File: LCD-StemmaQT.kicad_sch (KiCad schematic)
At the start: 18 parts, among them J101 STEMMA QT, J102 LCD, J103 BL enable, Q101 MMBT3904, U101 PCF8574TS

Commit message: Non functional corrections on PCB
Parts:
- JP101: value SolderJumper_2_Open -> A0
- JP102: value SolderJumper_2_Open -> A1
- JP103: value SolderJumper_2_Open -> A2
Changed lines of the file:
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@@
   )
   (symbol (lib_id "Device:R") (at 73.66 41.91 0) (unit 1)
-    (in_bom yes) (on_board yes) (fields_autoplaced)
+    (in_bom yes) (on_board yes)
     (property "Reference" "R105" (id 0) (at 75.565 40.6399 0)
       (effects (font (size 1.27 1.27)) (justify left))
@@
       (effects (font (size 1.27 1.27)) hide)
     )
-    (property "LCSC" "C25804" (id 4) (at 73.66 41.91 0))
+    (property "LCSC" "C25804" (id 4) (at 79.375 45.085 0))
     (pin "1")
     (pin "2")
@@
     )
     (property "Footprint" "Connector_PinHeader_2.54mm:PinHeader_1x16_P2.54mm_Vertical" (id 2) (at 252.73 97.1549 0)
-      (effects (font (size 1.27 1.27)) (justify left))
+      (effects (font (size 1.27 1.27)) (justify left) hide)
     )
     (property "Datasheet" "~" (id 3) (at 249.555 93.345 0)
@@
   )
   (symbol (lib_id "Interface_Expansion:PCF8574TS") (at 125.73 115.57 0) (unit 1)
-    (in_bom yes) (on_board yes) (fields_autoplaced)
-    (property "Reference" "U101" (id 0) (at 127.7494 95.25 0)
-      (effects (font (size 1.27 1.27)) (justify left))
-    )
-    (property "Value" "PCF8574TS" (id 1) (at 127.7494 97.79 0)
+    (in_bom yes) (on_board yes)
+    (property "Reference" "U101" (id 0) (at 127.7494 94.615 0)
+      (effects (font (size 1.27 1.27)) (justify left))
+    )
+    (property "Value" "PCF8574TS" (id 1) (at 127.7494 97.155 0)
       (effects (font (size 1.27 1.27)) (justify left))
     )
@@
       (effects (font (size 1.27 1.27)) hide)
     )
-    (property "LCSC" "C57790" (id 4) (at 125.73 115.57 0))
+    (property "LCSC" "C57790" (id 4) (at 131.445 99.06 0))
     (pin "1")
     (pin "10")
@@
   )
   (symbol (lib_id "Device:R") (at 64.135 41.91 0) (unit 1)
-    (in_bom yes) (on_board yes) (fields_autoplaced)
+    (in_bom yes) (on_board yes)
     (property "Reference" "R104" (id 0) (at 66.04 40.6399 0)
       (effects (font (size 1.27 1.27)) (justify left))
@@
       (effects (font (size 1.27 1.27)) hide)
     )
-    (property "LCSC" "C25804" (id 4) (at 64.135 41.91 0))
+    (property "LCSC" "C25804" (id 4) (at 69.85 45.085 0))
     (pin "1")
     (pin "2")
@@
   )
   (symbol (lib_id "Device:R") (at 100.33 41.91 0) (unit 1)
-    (in_bom yes) (on_board yes) (fields_autoplaced)
+    (in_bom yes) (on_board yes)
     (property "Reference" "R106" (id 0) (at 102.235 40.6399 0)
       (effects (font (size 1.27 1.27)) (justify left))
@@
       (effects (font (size 1.27 1.27)) hide)
     )
-    (property "LCSC" "C23162" (id 4) (at 100.33 41.91 0))
+    (property "LCSC" "C23162" (id 4) (at 106.045 45.085 0))
     (pin "1")
     (pin "2")
   )
   (symbol (lib_id "Device:R") (at 36.195 41.91 0) (unit 1)
-    (in_bom yes) (on_board yes) (fields_autoplaced)
+    (in_bom yes) (on_board yes)
     (property "Reference" "R102" (id 0) (at 38.1 40.6399 0)
       (effects (font (size 1.27 1.27)) (justify left))
@@
       (effects (font (size 1.27 1.27)) hide)
     )
-    (property "LCSC" "C21190" (id 4) (at 36.195 41.91 0))
+    (property "LCSC" "C21190" (id 4) (at 41.91 45.085 0))
     (pin "1")
     (pin "2")
@@
   )
   (symbol (lib_id "Transistor_BJT:MMBT3904") (at 187.325 59.69 0) (unit 1)
-    (in_bom yes) (on_board yes) (fields_autoplaced)
+    (in_bom yes) (on_board yes)
     (property "Reference" "Q101" (id 0) (at 193.04 58.4199 0)
       (effects (font (size 1.27 1.27)) (justify left))
@@
       (effects (font (size 1.27 1.27)) (justify left) hide)
     )
-    (property "LCSC" "C411758" (id 4) (at 187.325 59.69 0))
+    (property "LCSC" "C411758" (id 4) (at 197.485 63.5 0))
     (pin "1")
     (pin "2")
@@
   )
   (symbol (lib_id "Jumper:SolderJumper_2_Open") (at 64.135 59.69 90) (unit 1)
-    (in_bom yes) (on_board yes) (fields_autoplaced)
-    (property "Reference" "JP102" (id 0) (at 58.42 59.69 0))
-    (property "Value" "SolderJumper_2_Open" (id 1) (at 60.96 59.69 0)
-      (effects (font (size 1.27 1.27)) hide)
-    )
+    (in_bom yes) (on_board yes)
+    (property "Reference" "JP102" (id 0) (at 60.325 59.69 0))
+    (property "Value" "A1" (id 1) (at 62.23 59.69 0))
     (property "Footprint" "Jumper:SolderJumper-2_P1.3mm_Open_TrianglePad1.0x1.5mm" (id 2) (at 64.135 59.69 0)
       (effects (font (size 1.27 1.27)) hide)
@@
   )
   (symbol (lib_id "Device:R") (at 112.395 41.91 0) (unit 1)
-    (in_bom yes) (on_board yes) (fields_autoplaced)
+    (in_bom yes) (on_board yes)
     (property "Reference" "R107" (id 0) (at 114.3 40.6399 0)
       (effects (font (size 1.27 1.27)) (justify left))
@@
       (effects (font (size 1.27 1.27)) hide)
     )
-    (property "LCSC" "C23162" (id 4) (at 112.395 41.91 0))
+    (property "LCSC" "C23162" (id 4) (at 118.11 45.085 0))
     (pin "1")
     (pin "2")
   )
   (symbol (lib_id "Device:R") (at 53.975 41.91 0) (unit 1)
-    (in_bom yes) (on_board yes) (fields_autoplaced)
+    (in_bom yes) (on_board yes)
     (property "Reference" "R103" (id 0) (at 55.88 40.6399 0)
       (effects (font (size 1.27 1.27)) (justify left))
@@
       (effects (font (size 1.27 1.27)) hide)
     )
-    (property "LCSC" "C25804" (id 4) (at 53.975 41.91 0))
+    (property "LCSC" "C25804" (id 4) (at 59.69 45.085 0))
     (pin "1")
     (pin "2")
@@
   )
   (symbol (lib_id "Jumper:SolderJumper_2_Open") (at 73.66 59.69 90) (unit 1)
-    (in_bom yes) (on_board yes) (fields_autoplaced)
-    (property "Reference" "JP103" (id 0) (at 67.945 59.69 0))
-    (property "Value" "SolderJumper_2_Open" (id 1) (at 70.485 59.69 0)
-      (effects (font (size 1.27 1.27)) hide)
-    )
+    (in_bom yes) (on_board yes)
+    (property "Reference" "JP103" (id 0) (at 69.85 59.69 0))
+    (property "Value" "A2" (id 1) (at 71.755 59.69 0))
     (property "Footprint" "Jumper:SolderJumper-2_P1.3mm_Open_TrianglePad1.0x1.5mm" (id 2) (at 73.66 59.69 0)
       (effects (font (size 1.27 1.27)) hide)
@@
       (effects (font (size 1.27 1.27)) hide)
     )
-    (property "LCSC" "C23162" (id 4) (at 176.53 41.91 0))
+    (property "LCSC" "C23162" (id 4) (at 182.88 42.545 0))
     (pin "1")
     (pin "2")
@@
   (symbol (lib_id "Device:LED") (at 36.195 59.69 90) (unit 1)
     (in_bom yes) (on_board yes)
-    (property "Reference" "D101" (id 0) (at 29.21 61.2775 0))
-    (property "Value" "LED" (id 1) (at 31.75 61.2775 0))
+    (property "Reference" "D101" (id 0) (at 31.115 57.785 90))
+    (property "Value" "LED" (id 1) (at 30.48 60.325 90))
     (property "Footprint" "LED_SMD:LED_0603_1608Metric_Pad1.05x0.95mm_HandSolder" (id 2) (at 36.195 59.69 0)
       (effects (font (size 1.27 1.27)) hide)
@@
       (effects (font (size 1.27 1.27)) hide)
     )
-    (property "LCSC" "C2286" (id 4) (at 36.195 59.69 0))
+    (property "LCSC" "C2286" (id 4) (at 31.75 62.23 90))
     (pin "1")
     (pin "2")
@@
       (effects (font (size 1.27 1.27)) hide)
     )
-    (property "LCSC" "C14663" (id 4) (at 130.175 41.91 0))
+    (property "LCSC" "C14663" (id 4) (at 137.795 45.085 0))
     (pin "1")
     (pin "2")
   )
   (symbol (lib_id "Jumper:SolderJumper_2_Open") (at 53.975 59.69 90) (unit 1)
-    (in_bom yes) (on_board yes) (fields_autoplaced)
-    (property "Reference" "JP101" (id 0) (at 48.26 59.69 0))
-    (property "Value" "SolderJumper_2_Open" (id 1) (at 50.8 59.69 0)
-      (effects (font (size 1.27 1.27)) hide)
-    )
+    (in_bom yes) (on_board yes)
+    (property "Reference" "JP101" (id 0) (at 50.165 59.69 0))
+    (property "Value" "A0" (id 1) (at 52.07 59.69 0))
     (property "Footprint" "Jumper:SolderJumper-2_P1.3mm_Open_TrianglePad1.0x1.5mm" (id 2) (at 53.975 59.69 0)
       (effects (font (size 1.27 1.27)) hide)
@@
     )
     (path "/fcee0fb2-df32-4024-ba70-44a5ab719340"
-      (reference "JP101") (unit 1) (value "SolderJumper_2_Open") (footprint "Jumper:SolderJumper-2_P1.3mm_Open_TrianglePad1.0x1.5mm")
+      (reference "JP101") (unit 1) (value "A0") (footprint "Jumper:SolderJumper-2_P1.3mm_Open_TrianglePad1.0x1.5mm")
     )
     (path "/82161366-81a3-4ef5-a36a-e224ed535ca4"
-      (reference "JP102") (unit 1) (value "SolderJumper_2_Open") (footprint "Jumper:SolderJumper-2_P1.3mm_Open_TrianglePad1.0x1.5mm")
+      (reference "JP102") (unit 1) (value "A1") (footprint "Jumper:SolderJumper-2_P1.3mm_Open_TrianglePad1.0x1.5mm")
     )
     (path "/d61cd04e-b64c-459d-9e89-c068997ca3cf"
-      (reference "JP103") (unit 1) (value "SolderJumper_2_Open") (footprint "Jumper:SolderJumper-2_P1.3mm_Open_TrianglePad1.0x1.5mm")
+      (reference "JP103") (unit 1) (value "A2") (footprint "Jumper:SolderJumper-2_P1.3mm_Open_TrianglePad1.0x1.5mm")
     )
     (path "/5b3858e1-b0b8-469d-8aa5-091532f0b5b8"

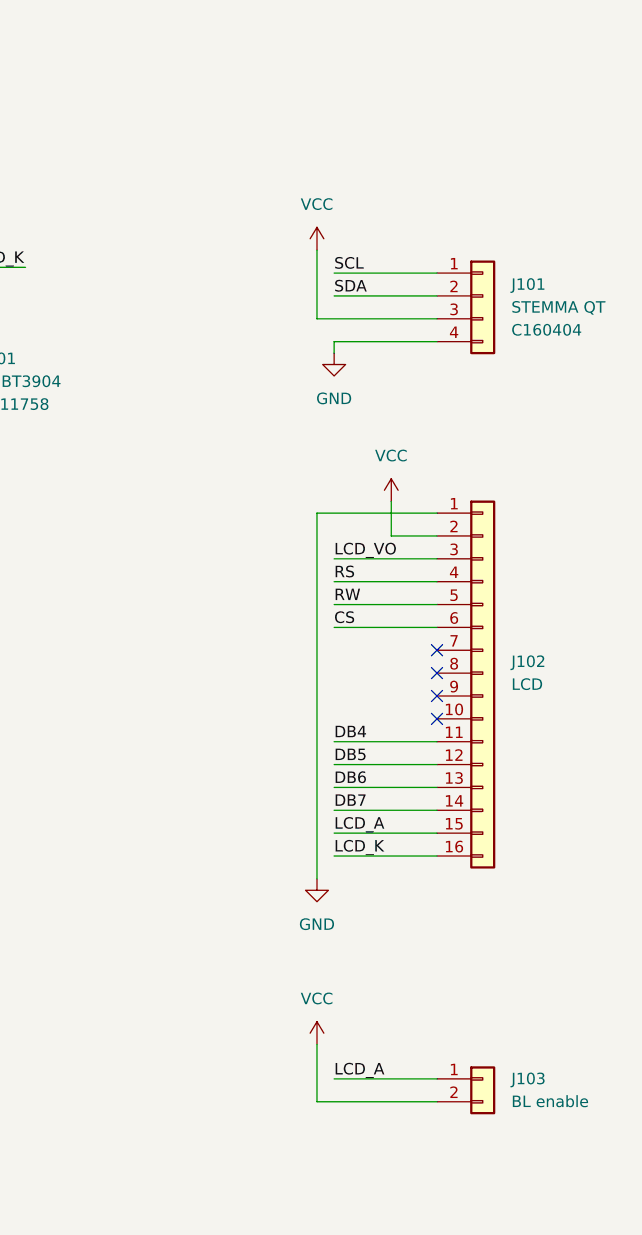
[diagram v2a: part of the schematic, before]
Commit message: Stemma QT footprint corrected
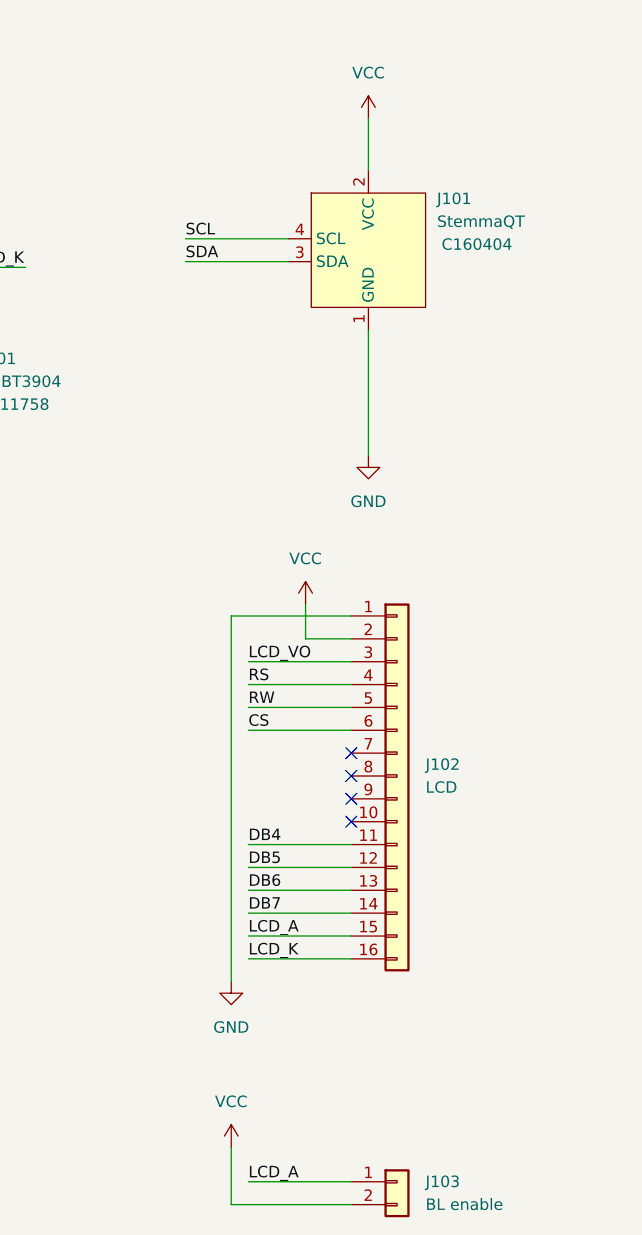
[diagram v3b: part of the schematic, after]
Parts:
- removed J101: STEMMA QT, Connector_JST:JST_SH_BM04B-SRSS-TB_1x04-1MP_P1.00mm_Vertical, symbol Connector_Generic:Conn_01x04
- added J101: StemmaQT, Connector_JST:JST_SH_SM04B-SRSS-TB_1x04-1MP_P1.00mm_Horizontal, symbol Resterampe:StemmaQT
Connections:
- net GND: now also J101.1 (GND)
- net SCL: now also J101.4 (SCL)
- net SDA: now also J101.3 (SDA)
- net VCC: now also J101.2 (VCC)
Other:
- moved on the sheet: J102, J103

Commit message: Documentation updated
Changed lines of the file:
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@@
   (junction (at 53.975 34.925) (diameter 0) (color 0 0 0 0)
+  )
+  (junction (at 215.9 86.995) (diameter 0) (color 0 0 0 0)
+  )
+  (junction (at 231.775 89.535) (diameter 0) (color 0 0 0 0)
   )
   (junction (at 53.975 48.26) (diameter 0) (color 0 0 0 0)
@@
     (stroke (width 0) (type default) (color 0 0 0 0))
   )
+  (wire (pts (xy 231.775 89.535) (xy 221.615 89.535))
+    (stroke (width 0) (type default) (color 0 0 0 0))
+  )
+  (wire (pts (xy 215.9 86.995) (xy 215.9 127.635))
+    (stroke (width 0) (type default) (color 0 0 0 0))
+  )
   (wire (pts (xy 53.975 34.925) (xy 53.975 38.1))
     (stroke (width 0) (type default) (color 0 0 0 0))
   )
-  (wire (pts (xy 234.95 86.995) (xy 221.615 86.995))
-    (stroke (width 0) (type default) (color 0 0 0 0))
-  )
-  (wire (pts (xy 229.87 89.535) (xy 229.87 85.725))
+  (wire (pts (xy 234.95 86.995) (xy 215.9 86.995))
+    (stroke (width 0) (type default) (color 0 0 0 0))
+  )
+  (wire (pts (xy 221.615 89.535) (xy 221.615 85.725))
     (stroke (width 0) (type default) (color 0 0 0 0))
   )
@@
     (stroke (width 0) (type default) (color 0 0 0 0))
   )
-  (wire (pts (xy 221.615 86.995) (xy 221.615 127.635))
-    (stroke (width 0) (type default) (color 0 0 0 0))
-  )
   (wire (pts (xy 100.33 45.72) (xy 100.33 48.26))
     (stroke (width 0) (type default) (color 0 0 0 0))
@@
     (stroke (width 0) (type default) (color 0 0 0 0))
   )
-  (wire (pts (xy 234.95 89.535) (xy 229.87 89.535))
+  (wire (pts (xy 234.95 89.535) (xy 231.775 89.535))
     (stroke (width 0) (type default) (color 0 0 0 0))
   )
@@
     (stroke (width 0) (type default) (color 0 0 0 0))
   )
+  (wire (pts (xy 210.82 86.995) (xy 210.82 85.725))
+    (stroke (width 0) (type default) (color 0 0 0 0))
+  )
   (wire (pts (xy 36.195 31.75) (xy 36.195 38.1))
     (stroke (width 0) (type default) (color 0 0 0 0))
@@
     (stroke (width 0) (type default) (color 0 0 0 0))
   )
+  (wire (pts (xy 215.9 86.995) (xy 210.82 86.995))
+    (stroke (width 0) (type default) (color 0 0 0 0))
+  )
   (wire (pts (xy 64.135 45.72) (xy 64.135 50.8))
     (stroke (width 0) (type default) (color 0 0 0 0))
@@
   )
   (wire (pts (xy 73.66 45.72) (xy 73.66 53.34))
+    (stroke (width 0) (type default) (color 0 0 0 0))
+  )
+  (wire (pts (xy 231.775 85.725) (xy 231.775 89.535))
     (stroke (width 0) (type default) (color 0 0 0 0))
   )
@@
     (pin "1")
   )
+  (symbol (lib_id "power:PWR_FLAG") (at 210.82 85.725 0) (unit 1)
+    (in_bom yes) (on_board yes) (fields_autoplaced)
+    (property "Reference" "#FLG0101" (id 0) (at 210.82 83.82 0)
+      (effects (font (size 1.27 1.27)) hide)
+    )
+    (property "Value" "PWR_FLAG" (id 1) (at 210.82 80.01 0))
+    (property "Footprint" "" (id 2) (at 210.82 85.725 0)
+      (effects (font (size 1.27 1.27)) hide)
+    )
+    (property "Datasheet" "~" (id 3) (at 210.82 85.725 0)
+      (effects (font (size 1.27 1.27)) hide)
+    )
+    (pin "1")
+  )
   (symbol (lib_id "power:VCC") (at 53.975 31.75 0) (unit 1)
     (in_bom yes) (on_board yes)
@@
     (pin "2")
   )
+  (symbol (lib_id "power:PWR_FLAG") (at 231.775 85.725 0) (unit 1)
+    (in_bom yes) (on_board yes) (fields_autoplaced)
+    (property "Reference" "#FLG0102" (id 0) (at 231.775 83.82 0)
+      (effects (font (size 1.27 1.27)) hide)
+    )
+    (property "Value" "PWR_FLAG" (id 1) (at 231.775 80.01 0))
+    (property "Footprint" "" (id 2) (at 231.775 85.725 0)
+      (effects (font (size 1.27 1.27)) hide)
+    )
+    (property "Datasheet" "~" (id 3) (at 231.775 85.725 0)
+      (effects (font (size 1.27 1.27)) hide)
+    )
+    (pin "1")
+  )
   (symbol (lib_id "power:VCC") (at 150.495 31.75 0) (unit 1)
     (in_bom yes) (on_board yes)
@@
     (pin "2")
   )
-  (symbol (lib_id "power:VCC") (at 229.87 85.725 0) (unit 1)
-    (in_bom yes) (on_board yes)
-    (property "Reference" "#PWR0115" (id 0) (at 229.87 89.535 0)
-      (effects (font (size 1.27 1.27)) hide)
-    )
-    (property "Value" "VCC" (id 1) (at 229.87 80.645 0))
-    (property "Footprint" "" (id 2) (at 229.87 85.725 0)
-      (effects (font (size 1.27 1.27)) hide)
-    )
-    (property "Datasheet" "" (id 3) (at 229.87 85.725 0)
+  (symbol (lib_id "power:VCC") (at 221.615 85.725 0) (unit 1)
+    (in_bom yes) (on_board yes)
+    (property "Reference" "#PWR0115" (id 0) (at 221.615 89.535 0)
+      (effects (font (size 1.27 1.27)) hide)
+    )
+    (property "Value" "VCC" (id 1) (at 221.615 80.645 0))
+    (property "Footprint" "" (id 2) (at 221.615 85.725 0)
+      (effects (font (size 1.27 1.27)) hide)
+    )
+    (property "Datasheet" "" (id 3) (at 221.615 85.725 0)
       (effects (font (size 1.27 1.27)) hide)
     )
@@
     (pin "1")
   )
-  (symbol (lib_id "power:GND") (at 221.615 127.635 0) (unit 1)
-    (in_bom yes) (on_board yes) (fields_autoplaced)
-    (property "Reference" "#PWR0117" (id 0) (at 221.615 133.985 0)
-      (effects (font (size 1.27 1.27)) hide)
-    )
-    (property "Value" "GND" (id 1) (at 221.615 132.715 0))
-    (property "Footprint" "" (id 2) (at 221.615 127.635 0)
-      (effects (font (size 1.27 1.27)) hide)
-    )
-    (property "Datasheet" "" (id 3) (at 221.615 127.635 0)
+  (symbol (lib_id "power:GND") (at 215.9 127.635 0) (unit 1)
+    (in_bom yes) (on_board yes) (fields_autoplaced)
+    (property "Reference" "#PWR0117" (id 0) (at 215.9 133.985 0)
+      (effects (font (size 1.27 1.27)) hide)
+    )
+    (property "Value" "GND" (id 1) (at 215.9 132.715 0))
+    (property "Footprint" "" (id 2) (at 215.9 127.635 0)
+      (effects (font (size 1.27 1.27)) hide)
+    )
+    (property "Datasheet" "" (id 3) (at 215.9 127.635 0)
       (effects (font (size 1.27 1.27)) hide)
     )
@@
   )
   (symbol_instances
+    (path "/2ea5e485-ea31-40af-a953-48226ca64cc2"
+      (reference "#FLG0101") (unit 1) (value "PWR_FLAG") (footprint "")
+    )
+    (path "/35342d17-66cb-463a-b374-5f3155f435a8"
+      (reference "#FLG0102") (unit 1) (value "PWR_FLAG") (footprint "")
+    )
     (path "/9977ece3-5ccb-4e4b-b184-6fb1ec008978"
       (reference "#PWR0101") (unit 1) (value "VCC") (footprint "")
